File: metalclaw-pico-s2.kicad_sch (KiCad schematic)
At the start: 57 parts, among them J1 USB_C_Receptacle_USB2.0_14P, J2 Conn_01x05, U1 ESP32-S2, U2 MX25L3236FM2I-08G-TR, U3 APS6404L-3SQRx-SN, U5 XC6220B331MR, Y1 XRCGB40M000F1S2FR0

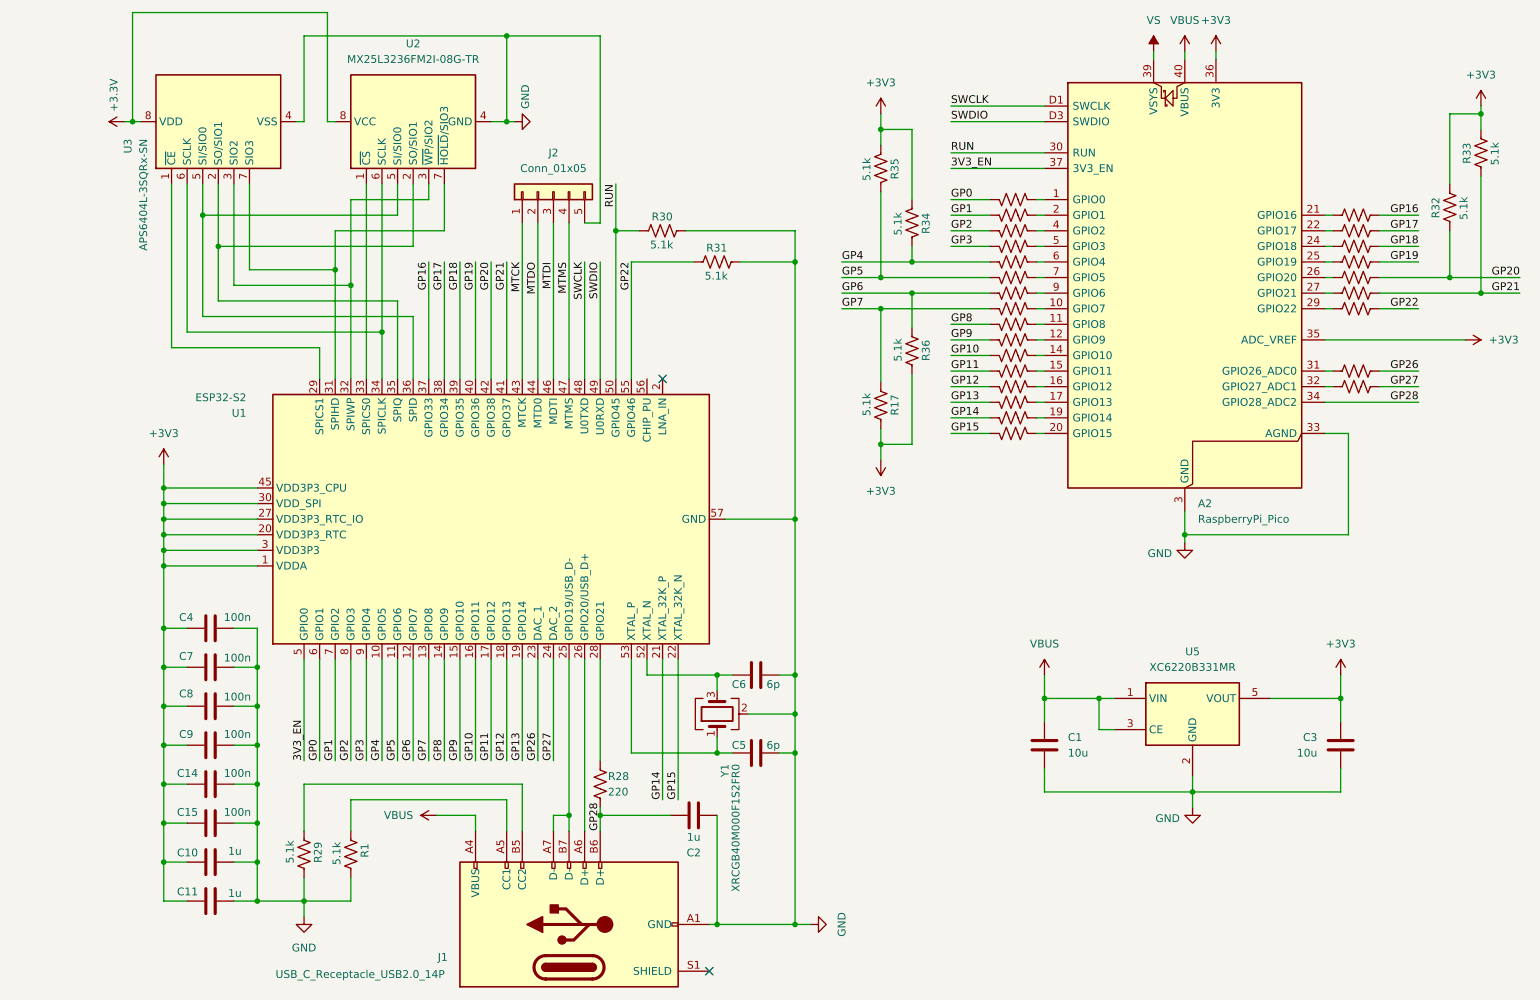
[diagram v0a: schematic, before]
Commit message: Rearrange schematic
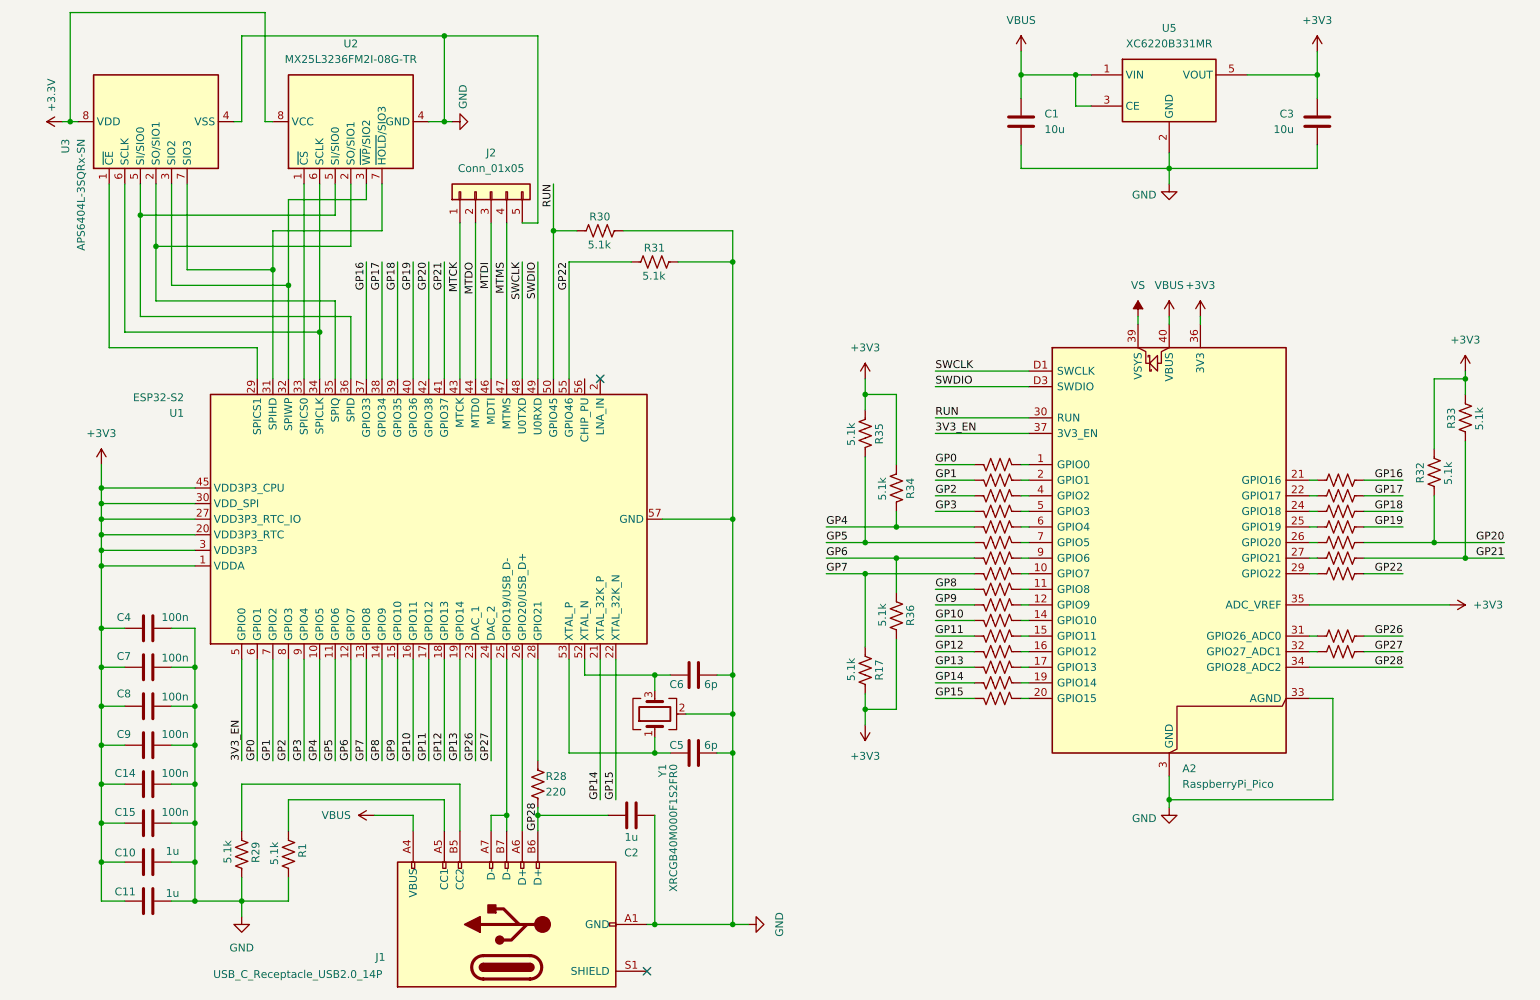
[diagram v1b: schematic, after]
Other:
- moved on the sheet: A2, C1, C10, C11, C14, C15, C2, C3, C4, C5, C6, C7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

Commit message: Add more I2C pins, JTAG connector
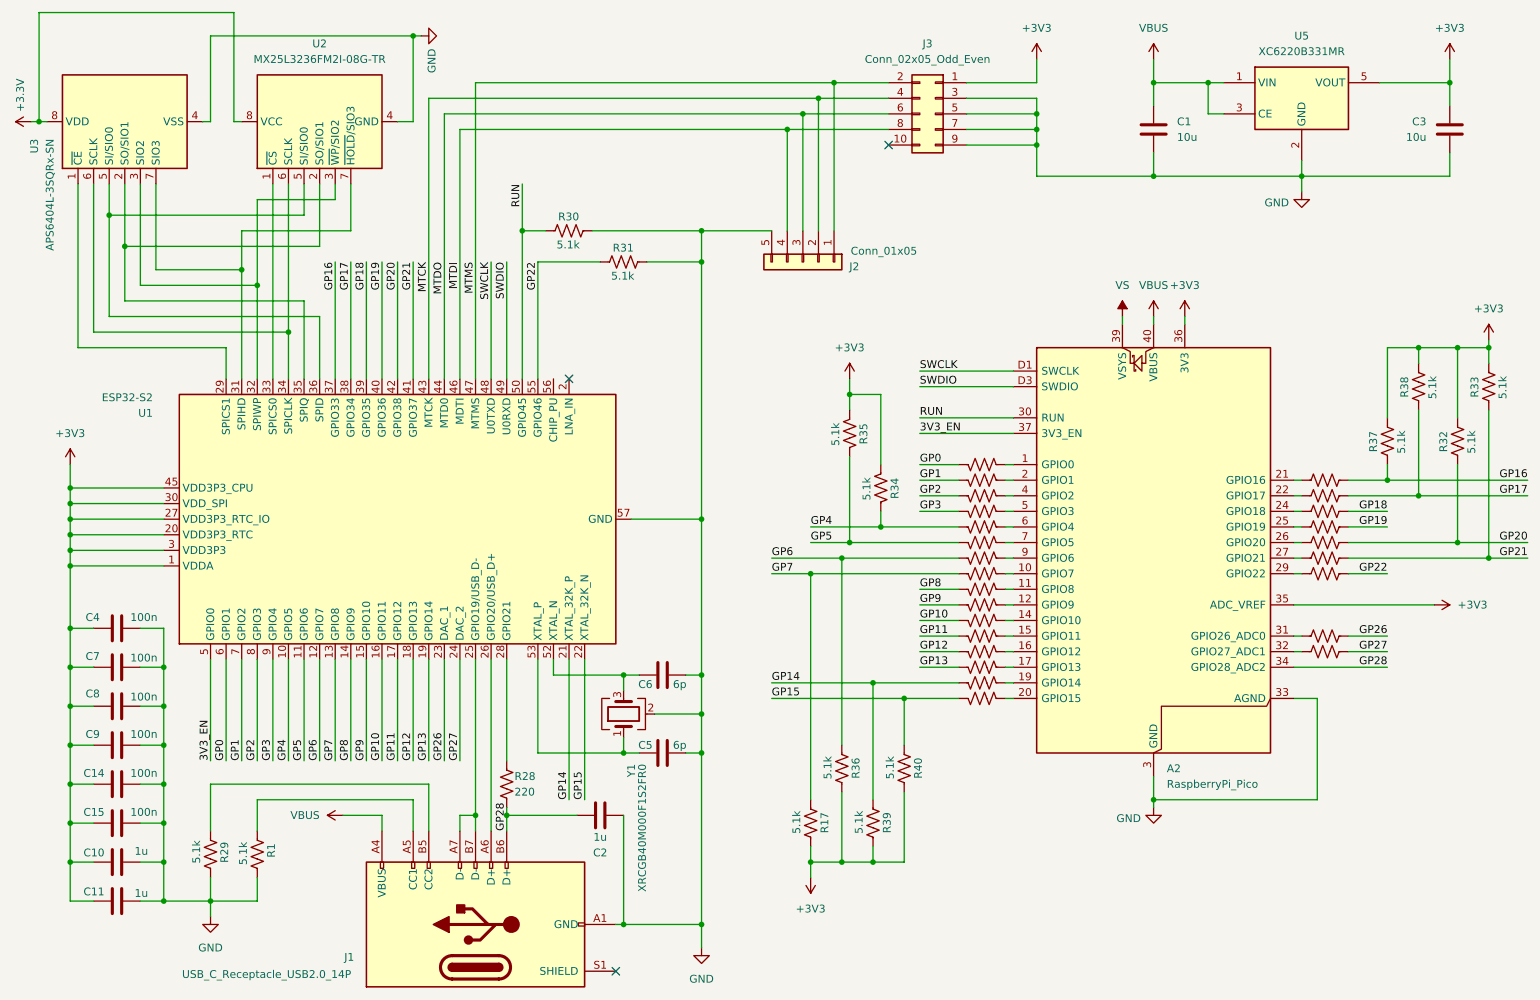
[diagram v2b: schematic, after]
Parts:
- added J3: Conn_02x05_Odd_Even, Connector_PinHeader_1.27mm:PinHeader_2x05_P1.27mm_Vertical_SMD, symbol Connector_Generic:Conn_02x05_Odd_Even
- added R37, R38, R39, R40: 5.1k, Capacitor_SMD:C_0402_1005Metric, symbol Device:R_US
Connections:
- net +3V3: now also J3.1 (Pin_1), R37.1, R38.1, R39.1, R40.1
- net GND: now also J3.3 (Pin_3), J3.5 (Pin_5), J3.7 (Pin_7), J3.9 (Pin_9)
- net GP14: now also R39.2
- net GP15: now also R40.2
- net GP16: now also R37.2
- net GP17: now also R38.2
- net MTCK: now also J2.2 (Pin_2), J3.4 (Pin_4); no longer J2.1 (Pin_1)
- net MTDI: now also J2.4 (Pin_4), J3.8 (Pin_8); no longer J2.3 (Pin_3)
- net MTDO: now also J2.3 (Pin_3), J3.6 (Pin_6); no longer J2.2 (Pin_2)
- net MTMS: now also J2.1 (Pin_1), J3.2 (Pin_2); no longer J2.4 (Pin_4)
- no-connect marks 2 -> 3
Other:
- moved on the sheet: A2, C1, C10, C11, C14, C15, C2, C3, C4, C5, C6, C7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

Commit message: Add footprint and parts for caps
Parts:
- C1, C3: footprint (none) -> Capacitor_SMD:C_0603_1608Metric; Mouser (none) -> 0603X106M100CT
- C5, C6: footprint (none) -> Capacitor_SMD:C_0402_1005Metric; Mouser (none) -> GRT1555C1H6R0DA02D
- R1, R10, R11, R12, R13, R14, R15, R16, R17, R18, R19, R2, R20, R21, R22, R23, R24, R25, R26, R27, R28, R29, R3, R30, R31, R32, R33, R34, R35, R36, R37, R38, R39, R4, R40, R5, R6, R7, R8, R9: footprint Capacitor_SMD:C_0402_1005Metric -> Resistor_SMD:R_01005_0402Metric
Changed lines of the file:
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@@
 			)
 		)
-		(property "Footprint" "Capacitor_SMD:C_0402_1005Metric"
+		(property "Footprint" "Resistor_SMD:R_01005_0402Metric"
 			(at 181.356 128.524 90)
 			(effects
@@
 			)
 		)
-		(property "Footprint" "Capacitor_SMD:C_0402_1005Metric"
+		(property "Footprint" "Resistor_SMD:R_01005_0402Metric"
 			(at 162.814 157.226 90)
 			(effects
@@
 			)
 		)
-		(property "Footprint" "Capacitor_SMD:C_0402_1005Metric"
+		(property "Footprint" "Resistor_SMD:R_01005_0402Metric"
 			(at 181.356 133.604 90)
 			(effects
@@
 			)
 		)
-		(property "Footprint" "Capacitor_SMD:C_0402_1005Metric"
+		(property "Footprint" "Resistor_SMD:R_01005_0402Metric"
 			(at 237.744 125.984 90)
 			(effects
@@
 			)
 		)
-		(property "Footprint" "Capacitor_SMD:C_0402_1005Metric"
+		(property "Footprint" "Resistor_SMD:R_01005_0402Metric"
 			(at 181.356 98.044 90)
 			(effects
@@
 			)
 		)
-		(property "Footprint" "Capacitor_SMD:C_0402_1005Metric"
+		(property "Footprint" "Resistor_SMD:R_01005_0402Metric"
 			(at 157.734 148.336 90)
 			(effects
@@
 			)
 		)
-		(property "Footprint" "Capacitor_SMD:C_0402_1005Metric"
+		(property "Footprint" "Resistor_SMD:R_01005_0402Metric"
 			(at 105.156 151.384 90)
 			(effects
@@
 			)
 		)
-		(property "Footprint" "Capacitor_SMD:C_0402_1005Metric"
+		(property "Footprint" "Resistor_SMD:R_01005_0402Metric"
 			(at 237.744 105.664 90)
 			(effects
@@
 			)
 		)
-		(property "Footprint" "Capacitor_SMD:C_0402_1005Metric"
+		(property "Footprint" "Resistor_SMD:R_01005_0402Metric"
 			(at 122.936 67.056 90)
 			(effects
@@
 			)
 		)
-		(property "Footprint" "Capacitor_SMD:C_0402_1005Metric"
+		(property "Footprint" "Resistor_SMD:R_01005_0402Metric"
 			(at 181.356 125.984 90)
 			(effects
@@
 			)
 		)
-		(property "Footprint" "Capacitor_SMD:C_0402_1005Metric"
+		(property "Footprint" "Resistor_SMD:R_01005_0402Metric"
 			(at 237.744 103.124 90)
 			(effects
@@
 			)
 		)
-		(property "Footprint" "Capacitor_SMD:C_0402_1005Metric"
+		(property "Footprint" "Resistor_SMD:R_01005_0402Metric"
 			(at 54.864 162.306 90)
 			(effects
@@
 			)
 		)
-		(property "Footprint" "Capacitor_SMD:C_0402_1005Metric"
+		(property "Footprint" "Resistor_SMD:R_01005_0402Metric"
 			(at 62.484 162.306 90)
 			(effects
@@
 			)
 		)
-		(property "Footprint" "Capacitor_SMD:C_0402_1005Metric"
+		(property "Footprint" "Resistor_SMD:R_01005_0402Metric"
 			(at 181.356 105.664 90)
 			(effects
@@
 			)
 		)
-		(property "Footprint" ""
+		(property "Footprint" "Capacitor_SMD:C_0603_1608Metric"
 			(at 210.5152 48.26 0)
 			(effects
@@
 			)
 		)
+		(property "Mouser" "0603X106M100CT"
+			(at 209.55 44.45 0)
+			(effects
+				(font
+					(size 1.27 1.27)
+				)
+				(hide yes)
+			)
+		)
 		(pin "1"
 		)
@@
 			)
 		)
-		(property "Footprint" "Capacitor_SMD:C_0402_1005Metric"
+		(property "Footprint" "Resistor_SMD:R_01005_0402Metric"
 			(at 181.356 120.904 90)
 			(effects
@@
 			)
 		)
-		(property "Footprint" ""
+		(property "Footprint" "Capacitor_SMD:C_0402_1005Metric"
 			(at 133.35 147.0152 0)
 			(effects
@@
 			)
 		)
+		(property "Mouser" "GRT1555C1H6R0DA02D"
+			(at 129.54 146.05 90)
+			(effects
+				(font
+					(size 1.27 1.27)
+				)
+				(hide yes)
+			)
+		)
 		(pin "2"
 		)
@@
 			)
 		)
-		(property "Footprint" "Capacitor_SMD:C_0402_1005Metric"
+		(property "Footprint" "Resistor_SMD:R_01005_0402Metric"
 			(at 181.356 108.204 90)
 			(effects
@@
 			)
 		)
-		(property "Footprint" "Capacitor_SMD:C_0402_1005Metric"
+		(property "Footprint" "Resistor_SMD:R_01005_0402Metric"
 			(at 181.356 136.144 90)
 			(effects
@@
 			)
 		)
-		(property "Footprint" "Capacitor_SMD:C_0402_1005Metric"
+		(property "Footprint" "Resistor_SMD:R_01005_0402Metric"
 			(at 164.084 103.124 90)
 			(effects
@@
 			)
 		)
-		(property "Footprint" ""
+		(property "Footprint" "Capacitor_SMD:C_0603_1608Metric"
 			(at 256.8448 48.26 0)
 			(effects
@@
 			)
 		)
+		(property "Mouser" "0603X106M100CT"
+			(at 257.81 44.45 0)
+			(effects
+				(font
+					(size 1.27 1.27)
+				)
+				(hide yes)
+			)
+		)
 		(pin "1"
 		)
@@
 			)
 		)
-		(property "Footprint" "Capacitor_SMD:C_0402_1005Metric"
+		(property "Footprint" "Resistor_SMD:R_01005_0402Metric"
 			(at 237.744 108.204 90)
 			(effects
@@
 			)
 		)
-		(property "Footprint" "Capacitor_SMD:C_0402_1005Metric"
+		(property "Footprint" "Resistor_SMD:R_01005_0402Metric"
 			(at 248.666 95.504 90)
 			(effects
@@
 			)
 		)
-		(property "Footprint" "Capacitor_SMD:C_0402_1005Metric"
+		(property "Footprint" "Resistor_SMD:R_01005_0402Metric"
 			(at 253.746 86.614 90)
 			(effects
@@
 			)
 		)
-		(property "Footprint" "Capacitor_SMD:C_0402_1005Metric"
+		(property "Footprint" "Resistor_SMD:R_01005_0402Metric"
 			(at 265.176 86.614 90)
 			(effects
@@
 			)
 		)
-		(property "Footprint" "Capacitor_SMD:C_0402_1005Metric"
+		(property "Footprint" "Resistor_SMD:R_01005_0402Metric"
 			(at 181.356 113.284 90)
 			(effects
@@
 			)
 		)
-		(property "Footprint" "Capacitor_SMD:C_0402_1005Metric"
+		(property "Footprint" "Resistor_SMD:R_01005_0402Metric"
 			(at 167.894 148.336 90)
 			(effects
@@
 			)
 		)
-		(property "Footprint" ""
+		(property "Footprint" "Capacitor_SMD:C_0402_1005Metric"
 			(at 133.35 132.3848 0)
 			(effects
@@
 			)
 		)
+		(property "Mouser" "GRT1555C1H6R0DA02D"
+			(at 129.54 133.35 90)
+			(effects
+				(font
+					(size 1.27 1.27)
+				)
+				(hide yes)
+			)
+		)
 		(pin "2"
 		)
@@
 			)
 		)
-		(property "Footprint" "Capacitor_SMD:C_0402_1005Metric"
+		(property "Footprint" "Resistor_SMD:R_01005_0402Metric"
 			(at 181.356 118.364 90)
 			(effects
@@
 			)
 		)
-		(property "Footprint" "Capacitor_SMD:C_0402_1005Metric"
+		(property "Footprint" "Resistor_SMD:R_01005_0402Metric"
 			(at 181.356 131.064 90)
 			(effects
@@
 			)
 		)
-		(property "Footprint" "Capacitor_SMD:C_0402_1005Metric"
+		(property "Footprint" "Resistor_SMD:R_01005_0402Metric"
 			(at 181.356 110.744 90)
 			(effects
@@
 			)
 		)
-		(property "Footprint" "Capacitor_SMD:C_0402_1005Metric"
+		(property "Footprint" "Resistor_SMD:R_01005_0402Metric"
 			(at 237.744 110.744 90)
 			(effects
@@
 			)
 		)
-		(property "Footprint" "Capacitor_SMD:C_0402_1005Metric"
+		(property "Footprint" "Resistor_SMD:R_01005_0402Metric"
 			(at 159.004 94.234 90)
 			(effects
@@
 			)
 		)
-		(property "Footprint" "Capacitor_SMD:C_0402_1005Metric"
+		(property "Footprint" "Resistor_SMD:R_01005_0402Metric"
 			(at 114.046 61.976 90)
 			(effects
@@
 			)
 		)
-		(property "Footprint" "Capacitor_SMD:C_0402_1005Metric"
+		(property "Footprint" "Resistor_SMD:R_01005_0402Metric"
 			(at 237.744 100.584 90)
 			(effects
@@
 			)
 		)
-		(property "Footprint" "Capacitor_SMD:C_0402_1005Metric"
+		(property "Footprint" "Resistor_SMD:R_01005_0402Metric"
 			(at 181.356 115.824 90)
 			(effects
@@
 			)
 		)
-		(property "Footprint" "Capacitor_SMD:C_0402_1005Metric"
+		(property "Footprint" "Resistor_SMD:R_01005_0402Metric"
 			(at 237.744 113.284 90)
 			(effects
@@
 			)
 		)
-		(property "Footprint" "Capacitor_SMD:C_0402_1005Metric"
+		(property "Footprint" "Resistor_SMD:R_01005_0402Metric"
 			(at 237.744 115.824 90)
 			(effects
@@
 			)
 		)
-		(property "Footprint" "Capacitor_SMD:C_0402_1005Metric"
+		(property "Footprint" "Resistor_SMD:R_01005_0402Metric"
 			(at 260.096 95.504 90)
 			(effects
@@
 			)
 		)
-		(property "Footprint" "Capacitor_SMD:C_0402_1005Metric"
+		(property "Footprint" "Resistor_SMD:R_01005_0402Metric"
 			(at 181.356 103.124 90)
 			(effects
@@
 			)
 		)
-		(property "Footprint" "Capacitor_SMD:C_0402_1005Metric"
+		(property "Footprint" "Resistor_SMD:R_01005_0402Metric"
 			(at 181.356 100.584 90)
 			(effects
@@
 			)
 		)
-		(property "Footprint" "Capacitor_SMD:C_0402_1005Metric"
+		(property "Footprint" "Resistor_SMD:R_01005_0402Metric"
 			(at 152.654 157.226 90)
 			(effects
@@
 			)
 		)
-		(property "Footprint" "Capacitor_SMD:C_0402_1005Metric"
+		(property "Footprint" "Resistor_SMD:R_01005_0402Metric"
 			(at 237.744 128.524 90)
 			(effects
@@
 			)
 		)
-		(property "Footprint" "Capacitor_SMD:C_0402_1005Metric"
+		(property "Footprint" "Resistor_SMD:R_01005_0402Metric"
 			(at 181.356 123.444 90)
 			(effects

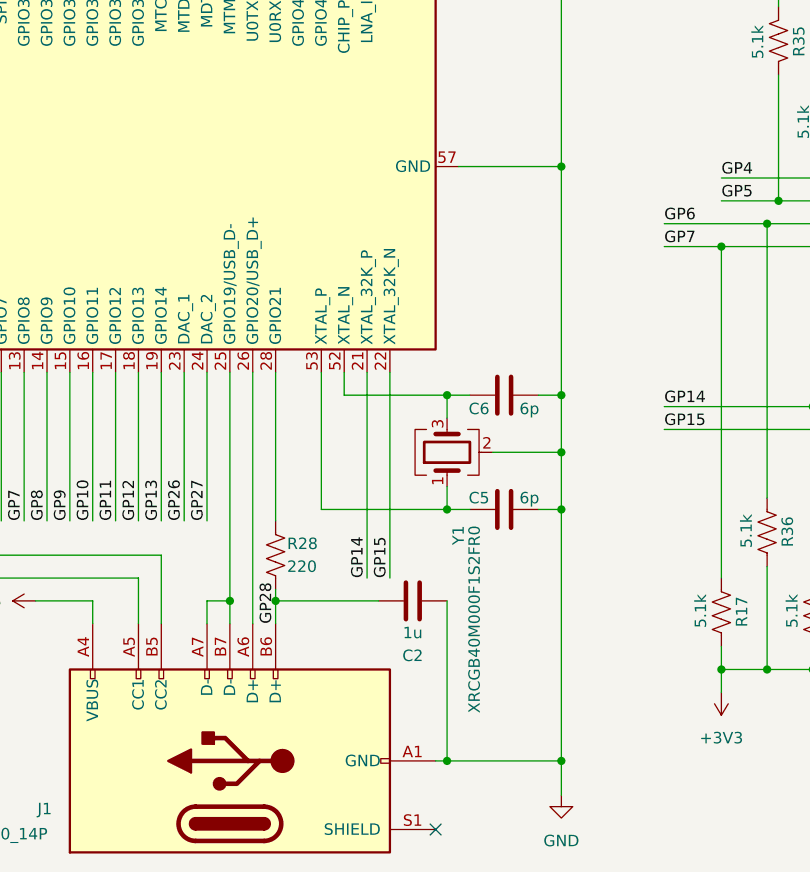
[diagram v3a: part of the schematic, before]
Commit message: Place resistors in rough areas
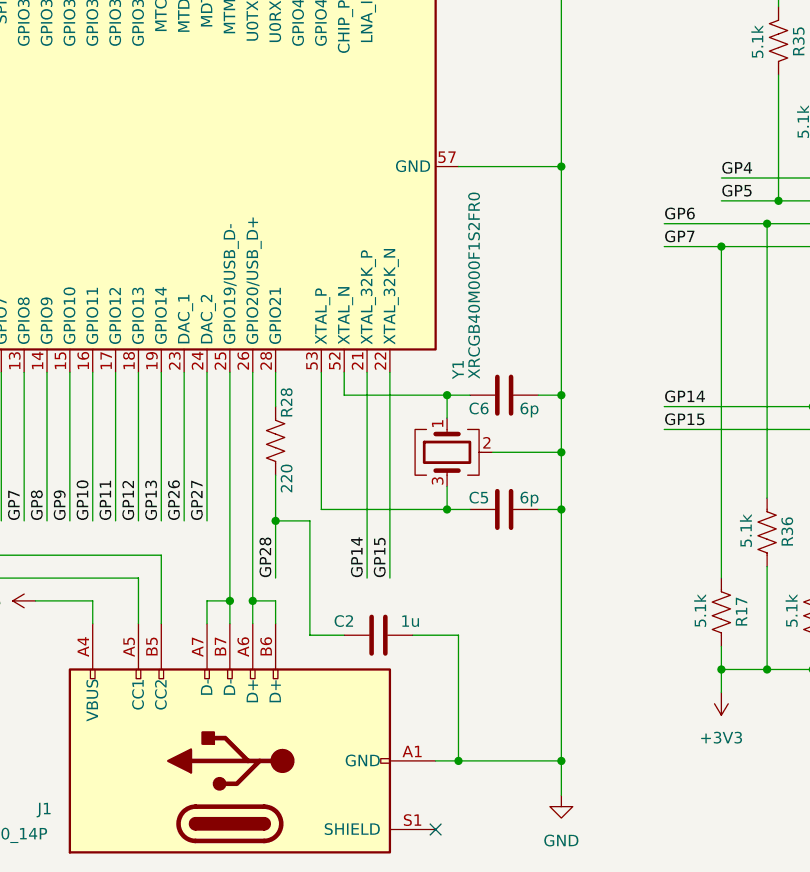
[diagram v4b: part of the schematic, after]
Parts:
- R1, R10, R11, R12, R13, R14, R15, R16, R17, R18, R19, R2, R20, R21, R22, R23, R24, R25, R26, R27, R28, R29, R3, R30, R31, R32, R33, R34, R35, R36, R37, R38, R39, R4, R40, R5, R6, R7, R8, R9: footprint Resistor_SMD:R_01005_0402Metric -> Resistor_SMD:R_0402_1005Metric
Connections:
- net GP28: no longer J1.B6 (D+)
- net at C5.1, U1.53 (XTAL_P): now also Y1.3; no longer Y1.1
- net at C6.1, U1.52 (XTAL_N): now also Y1.1; no longer Y1.3
- net at J1.A6 (D+), U1.26 (GPIO20/USB_D+): now also J1.B6 (D+)
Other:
- moved on the sheet: C2, R28
